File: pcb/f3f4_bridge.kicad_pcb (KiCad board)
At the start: 2 copper layers, 25.5 x 26.5 mm, 24 parts, among them J1 Screw_Terminal_01x02, J2 USB_C_Receptacle_USB2.0_14P, J3 Conn_01x05_Pin, J4 USB_B_Micro, U1 THVD8000, U2 STM32F042K6Ux, U3 TLV70033_SOT23-5

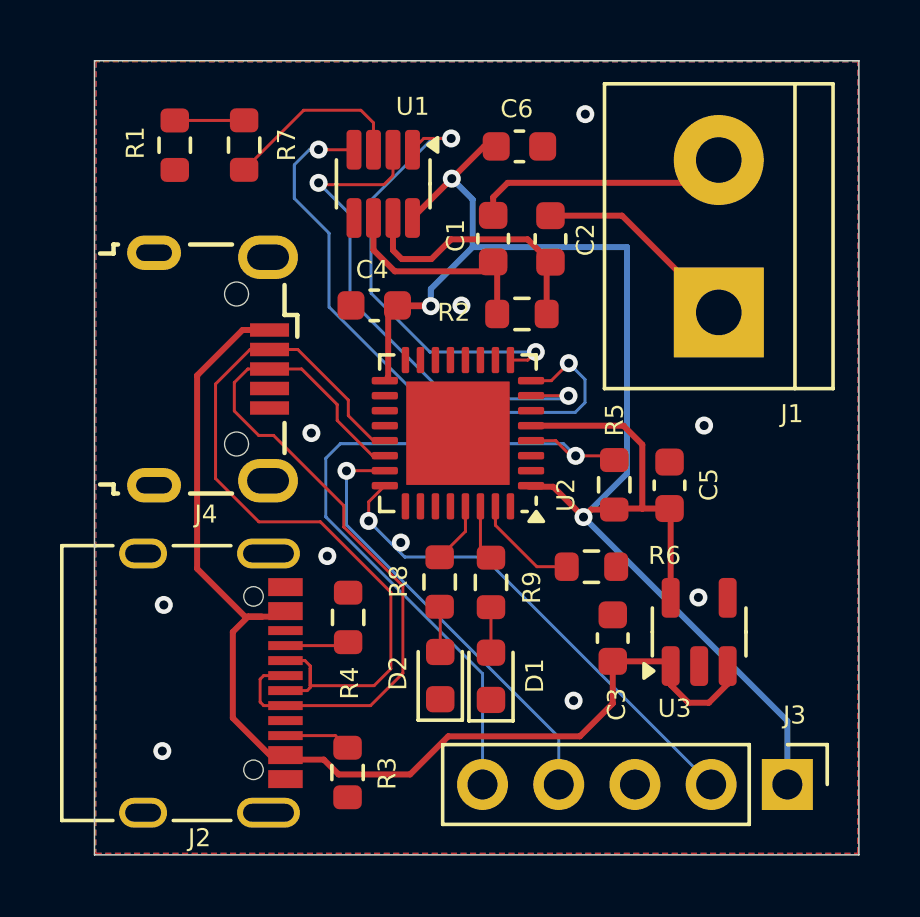
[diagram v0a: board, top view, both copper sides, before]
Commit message: add back to STM32 bootloader (masserase) add rule to flash using dfu-util fix led lighting
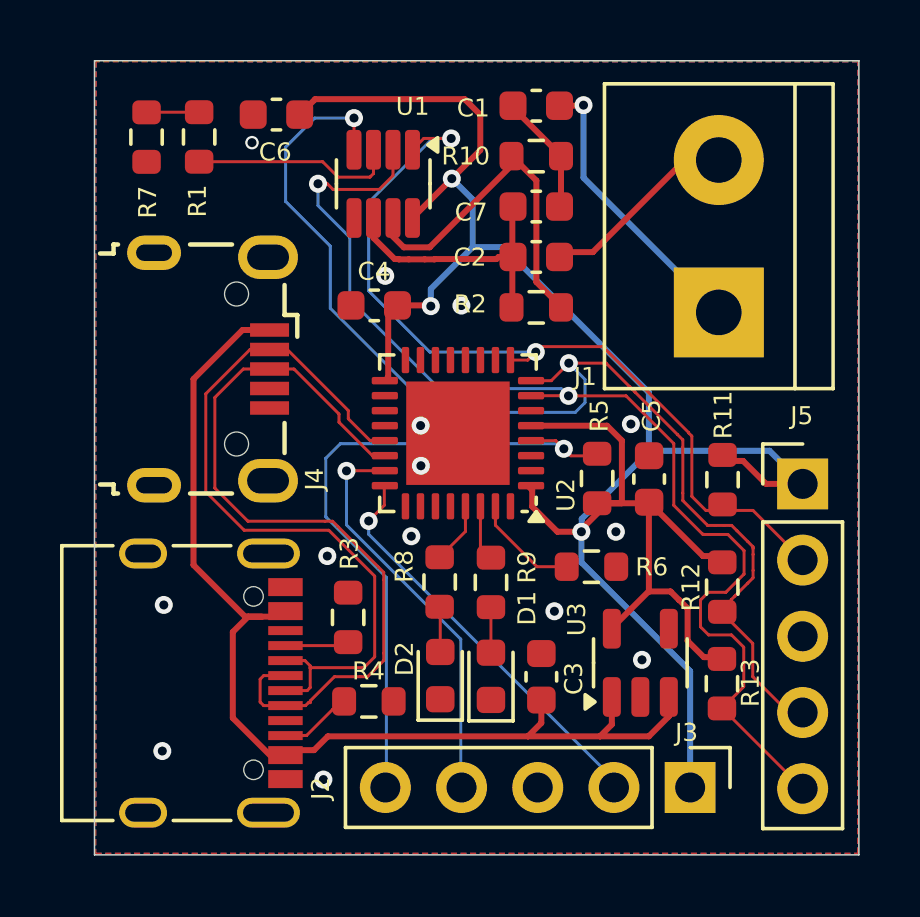
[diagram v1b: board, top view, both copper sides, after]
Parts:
- added C7: 10nF, Capacitor_SMD:C_0603_1608Metric, F.Cu at (43.2, 26.6)
- added J5: Conn_01x05, Connector_PinHeader_2.54mm:PinHeader_1x05_P2.54mm_Vertical, F.Cu at (52.1, 35.9)
- added R10: 82, Resistor_SMD:R_0603_1608Metric, F.Cu at (43.2, 24.9)
- added R11: 4.7k, Resistor_SMD:R_0603_1608Metric, F.Cu at (49.4, 35.7)
- added R12: 4.7k, Resistor_SMD:R_0603_1608Metric, F.Cu at (49.4, 39.3)
- added R13: 4.7k, Resistor_SMD:R_0603_1608Metric, F.Cu at (49.4, 42.5)
- R2: value 330 -> 120
- R7: value 820 -> 3k
- moved C6 8.17 mm to (34.6, 23.6), turned to 0 degrees
- moved C1 4.47 mm to (43.2, 23.3), turned to 0 degrees
- moved J3 3.24 mm to (48.4, 46.0)
- moved C3 2.71 mm to (43.4, 42.3)
- moved R3 2.47 mm to (37.6, 43.1), turned to 0 degrees
- moved U3 2.21 mm to (46.7, 41.8)
- moved C2 1.56 mm to (43.2, 28.3), turned to 0 degrees
- moved R1 1.52 mm to (32.0, 24.3)
- moved R7 0.98 mm to (30.2, 24.3)
- moved C5 0.71 mm to (47.0, 35.7)
- moved R5 0.61 mm to (45.3, 35.7)
- moved R2 0.53 mm to (43.2, 30.0)
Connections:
- C1 pad 1: Net-(U1-B) -> Net-(C1-Pad1)
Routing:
- net /UART_TXEN: track 17.8 -> 38.7 mm
- net /VCC: track 54.8 -> 75.6 mm
- net /UART_TX: track 20.6 -> 40.0 mm
- net /UART_RX: track 15.3 -> 28.5 mm
- net Net-(C1-Pad1): track 0.00 -> 4.12 mm
- net Net-(U1-B): track 8.81 -> 11.9 mm
- net /SWDCLK: track 16.5 -> 13.7 mm
- net Net-(J1-Pin_1): track 6.95 -> 9.60 mm, vias 0 -> 1
- net /NRST: track 24.8 -> 22.6 mm
- net /VBUS: track 38.6 -> 36.5 mm
- net Net-(J1-Pin_2): track 8.64 -> 6.57 mm
- net Net-(U1-A): track 7.27 -> 8.94 mm
- net /SWDIO: track 14.7 -> 13.4 mm
- net /USBDM: track 26.8 -> 25.6 mm
- net /USBDP: track 25.9 -> 26.7 mm
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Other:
- board text added: "NASALINK R2"
- board text added: "RX"
- board text added: "TX"
- board text added: "TXEN"

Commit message: fix invalid inverted rx and tx leds
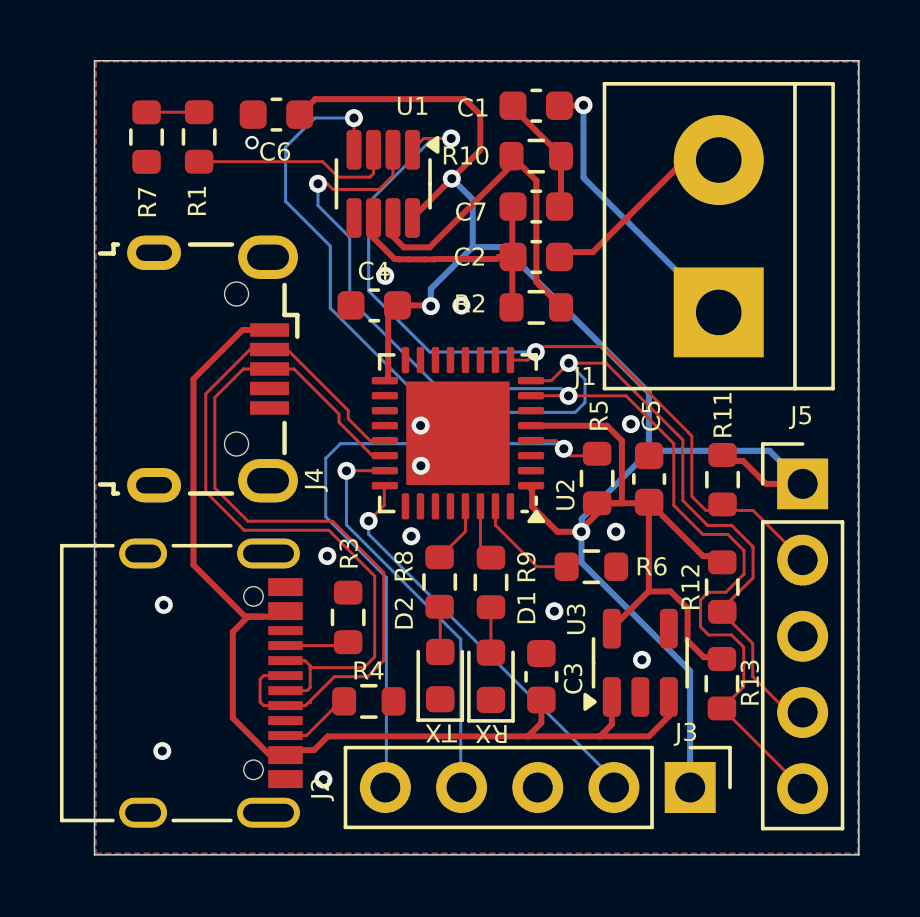
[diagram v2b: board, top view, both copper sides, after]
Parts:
- R1: value 47k -> 50k
- R7: value 3k -> 0
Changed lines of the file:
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@@
 			)
 		)
-		(property "Value" "3k"
+		(property "Value" "0"
 			(at -0.000001 1.429999 90)
 			(layer "F.Fab")
@@
 			)
 		)
-		(property "Value" "47k"
+		(property "Value" "50k"
 			(at 0.000001 1.429999 90)
 			(layer "F.Fab")
@@
 		(tags "LED")
 		(property "Reference" "D2"
-			(at 0.559999 -1.189999 90)
+			(at 2.069999 -1.189999 90)
 			(layer "F.SilkS")
 			(effects
@@
 		(sheetname "/")
 		(sheetfile "f3f4_bridge.kicad_sch")
-		(attr smd exclude_from_pos_files exclude_from_bom)
+		(attr smd exclude_from_pos_files)
 		(fp_line
 			(start 3.849999 3.749999)
@@
 		(layer "Edge.Cuts")
 	)
+	(gr_text "TX"
+		(at 40.05 44.16 180)
+		(layer "F.SilkS")
+		(effects
+			(font
+				(size 0.6 0.6)
+				(thickness 0.1)
+			)
+		)
+	)
+	(gr_text "RX"
+		(at 41.75 44.18 180)
+		(layer "F.SilkS")
+		(effects
+			(font
+				(size 0.6 0.6)
+				(thickness 0.1)
+			)
+		)
+	)
 	(gr_text "GND"
